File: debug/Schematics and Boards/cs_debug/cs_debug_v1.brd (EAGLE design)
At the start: 38.1 x 44.5 mm, 59 parts, among them J401 J-USB-HIROSE-MICRO-USB, Y101 32.768kHz, Y102 12mHz-12pF-K7

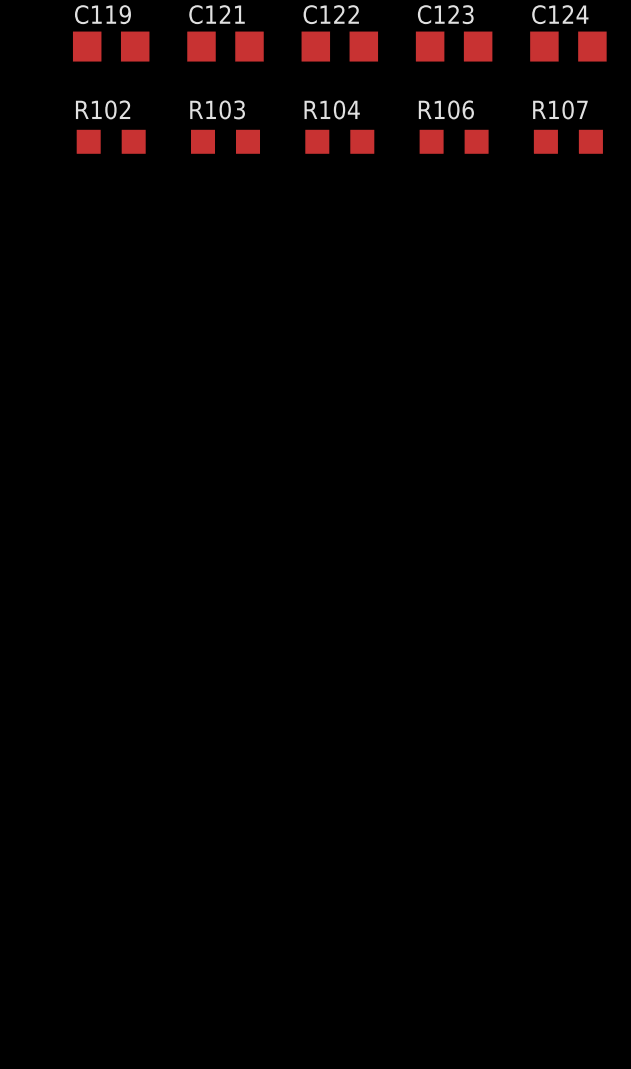
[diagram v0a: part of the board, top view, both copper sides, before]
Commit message: Add amplifiers and passives for high-side current monitor
FETs still to be added. Haven't set values on passives or added any part numbers to the circuit. Still need to convert the whole thing into a group. The nets have been named, and a few notes left behind for the remaining task
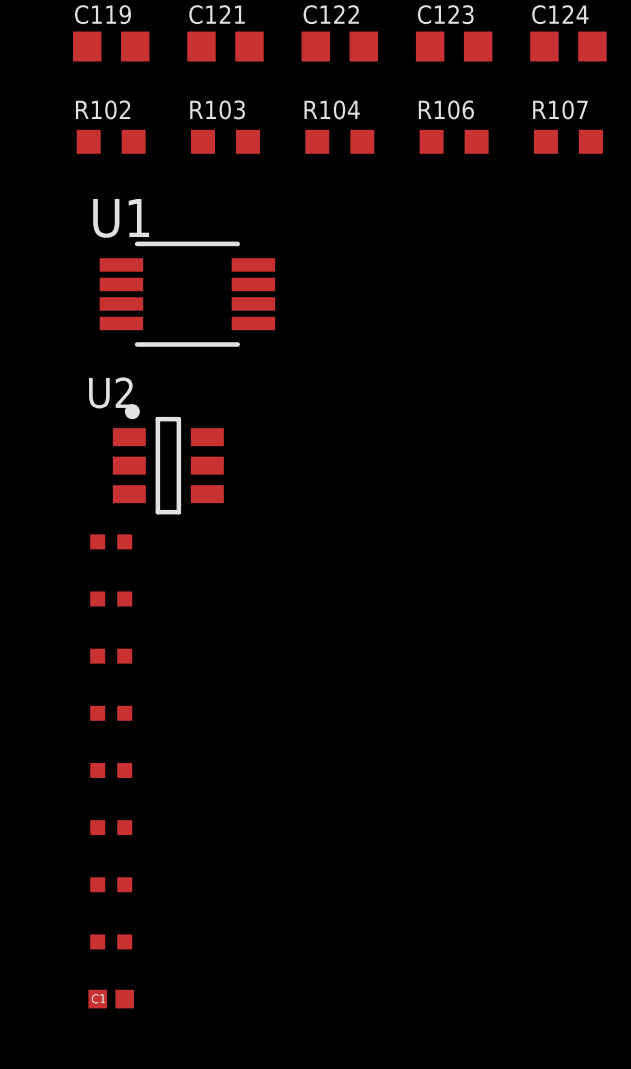
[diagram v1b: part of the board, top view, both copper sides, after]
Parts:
- added C1: (no value), Capacitors:C0402
- added R1, R2, R3, R4, R5, R6, R7, R8: (no value), Resistors:R0402
- added U1: INA225AIDGK, Amplifiers:DGK-MSOP8_INA225
- added U2: OPA357AIDBVTG4, Amplifiers:OPA357AIDBVTG4
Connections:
- new net AGND: R5.1, U1.GND, U1.REF, U2.VREF-
- new net DCBIAS_SHUTDOWN: R6.1
- new net DIFFAMP_GAIN0: U1.GS0
- new net DIFFAMP_GAIN1: U1.GS1
- new net N$1: R1.2, R2.2, U2.IN+
- new net N$3: U1.OUT
- new net N$4: R3.1, U2.ENABLE
- new net N$6: R4.1, R5.2, U2.IN-
- new net N$7: R4.2, R7.1, U2.OUT
- new net N$8: C1.2, R8.2, U1.IN+
- new net N$9: C1.1, R7.2, U1.IN-
- new net V_OFFSET_IN: R1.1
- new net V_SENSE_N: R2.1
- new net V_SENSE_P: R8.1
- net 3V3_INSTR_PROC: now also R3.2, R6.2, U1.VS, U2.VREF+

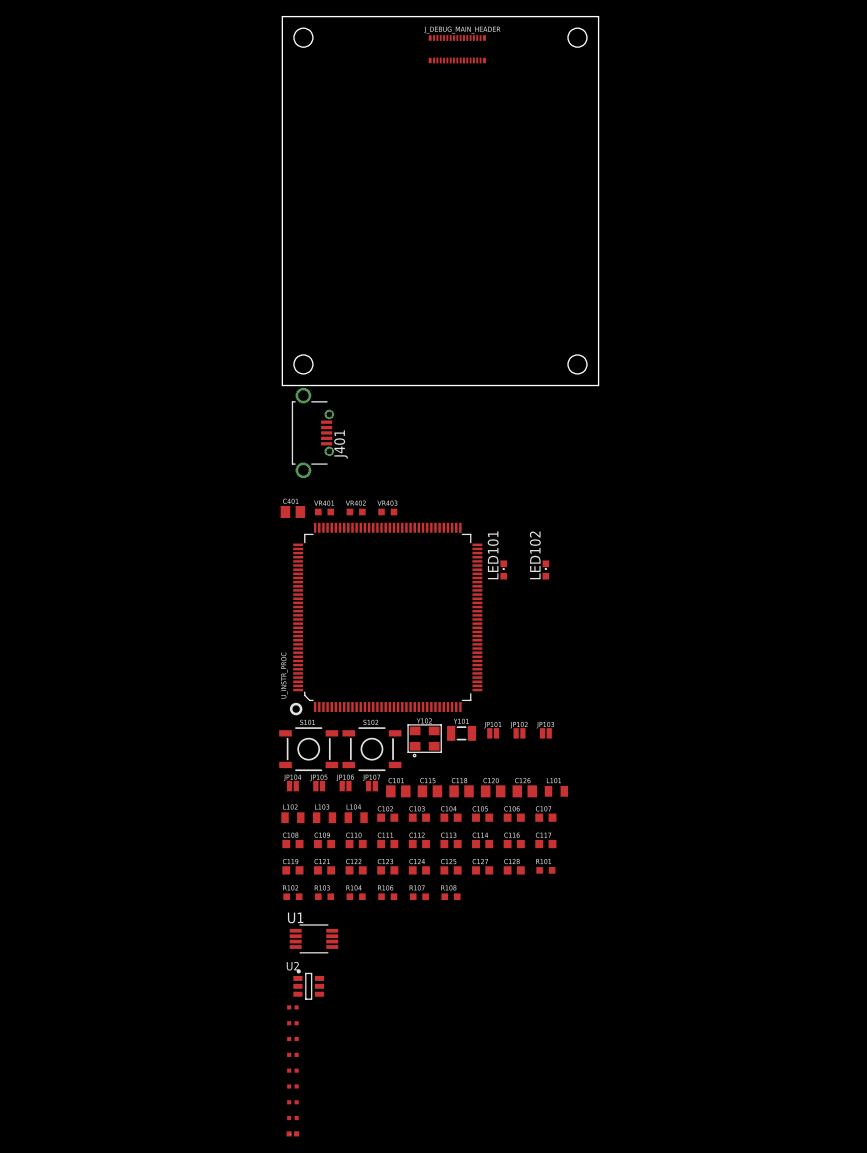
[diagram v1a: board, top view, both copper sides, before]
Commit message: Add high side current monitors as groups; label pins from main connector
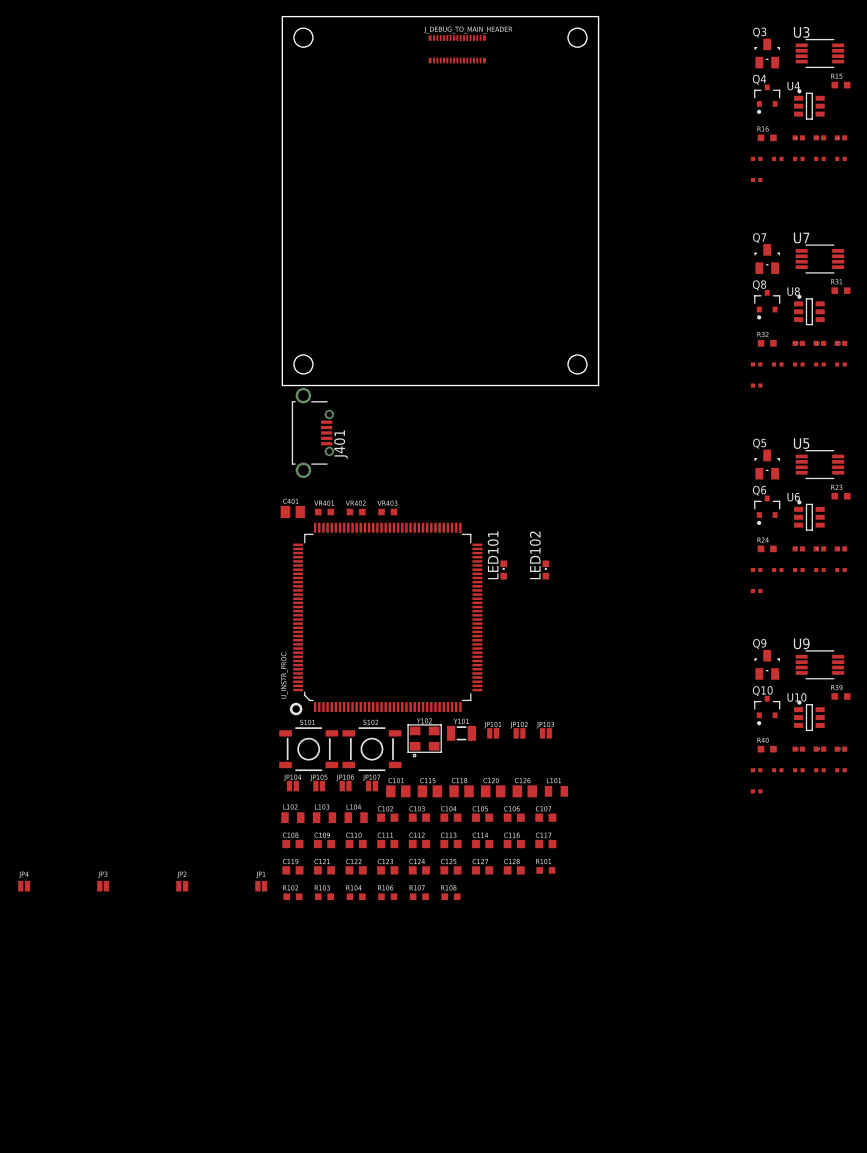
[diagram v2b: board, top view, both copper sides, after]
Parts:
- removed C1: (no value), Capacitors:C0402
- removed R1, R2, R3, R4, R5, R6, R7, R8: (no value), Resistors:R0402
- removed U1: INA225AIDGK, Amplifiers:DGK-MSOP8_INA225
- removed U2: OPA357AIDBVTG4, Amplifiers:OPA357AIDBVTG4
- added C10, C13, C4, C7: 68p, Capacitors:C0402
- added C11, C12, C14, C15, C5, C6, C8, C9: 0.1u, Capacitors:C0402
- added JP1, JP2, JP3, JP4: JUMPER-SMT_2_NC_PASTE_NO-SILK, SparkFun-Jumpers:SMT-JUMPER_2_NC_PASTE_NO-SILK
- added Q10, Q4, Q6, Q8: 2N7002P, Switches:SOT23-3_2N7002P
- added Q3, Q5, Q7, Q9: FDN340P, Switches:SOT23-3_FDN340P
- added R10, R12, R14, R18, R20, R22, R26, R28, R30, R34, R36, R38: 10k, Resistors:R0402
- added R11, R19, R27, R35: 100k, Resistors:R0402
- added R13, R17, R21, R25, R29, R33, R37, R9: 249k, Resistors:R0402
- added R15, R16, R23, R24, R31, R32, R39, R40: 5.1, Resistors:R0603
- added U10, U4, U6, U8: OPA357AIDBVTG4, Amplifiers:OPA357AIDBVTG4
- added U3, U5, U7, U9: INA225AIDGK, Amplifiers:DGK-MSOP8_INA225
- renumbered J_DEBUG_MAIN_HEADER to J_DEBUG_TO_MAIN_HEADER
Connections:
- removed net DCBIAS_SHUTDOWN: R6.1
- removed net DIFFAMP_GAIN0: U1.GS0
- removed net DIFFAMP_GAIN1: U1.GS1
- removed net N$1: R1.2, R2.2, U2.IN+
- removed net N$3: U1.OUT
- removed net N$4: R3.1, U2.ENABLE
- removed net N$6: R4.1, R5.2, U2.IN-
- removed net N$7: R4.2, R7.1, U2.OUT
- removed net N$8: C1.2, R8.2, U1.IN+
- removed net N$9: C1.1, R7.2, U1.IN-
- removed net V_OFFSET_IN: R1.1
- removed net V_SENSE_N: R2.1
- new net CM_DTR_DCBIAS_SHUTDOWN: Q8.G, R30.1
- new net CM_DTR_DIFFAMP_GAIN0: U7.GS0
- new net CM_DTR_DIFFAMP_GAIN1: U7.GS1
- new net CM_DTR_DIFFAMP_N3: C10.1, R31.2, U7.IN-
- new net CM_DTR_DIFFAMP_OUT: U7.OUT
- new net CM_DTR_DIFFAMP_P3: C10.2, R32.2, U7.IN+
- new net CM_DTR_OPAMP_ENABLE3: Q7.G, Q8.D, R27.1, U8.ENABLE
- new net CM_DTR_OPAMP_N3: R28.1, R29.2, U8.IN-
- new net CM_DTR_OPAMP_OUT3: Q7.S, R28.2, R31.1, U8.OUT
- new net CM_DTR_OPAMP_P3: R25.2, R26.2, U8.IN+
- new net CM_DTR_V_OFFSET_IN: R25.1
- new net CM_DTR_V_SENSE_N: J_DEBUG_TO_MAIN_HEADER.16, Q7.D, R26.1
- new net CM_DTR_V_SENSE_P: JP4.2, R32.1
- new net CM_PROC_DCBIAS_SHUTDOWN: Q4.G, R14.1
- new net CM_PROC_DIFFAMP_GAIN0: U3.GS0
- new net CM_PROC_DIFFAMP_GAIN1: U3.GS1
- new net CM_PROC_DIFFAMP_N1: C4.1, R15.2, U3.IN-
- new net CM_PROC_DIFFAMP_OUT: U3.OUT
- new net CM_PROC_DIFFAMP_P1: C4.2, R16.2, U3.IN+
- new net CM_PROC_OPAMP_ENABLE1: Q3.G, Q4.D, R11.1, U4.ENABLE
- new net CM_PROC_OPAMP_N1: R12.1, R13.2, U4.IN-
- new net CM_PROC_OPAMP_OUT1: Q3.S, R12.2, R15.1, U4.OUT
- new net CM_PROC_V_OFFSET_IN: R9.1
- new net CM_PROC_V_SENSE_N: J_DEBUG_TO_MAIN_HEADER.14, Q3.D, R10.1
- new net CM_PROC_V_SENSE_P: JP1.2, R16.1
- new net CM_STORAGE_DCBIAS_SHUTDOWN: Q6.G, R22.1
- new net CM_STORAGE_DIFFAMP_GAIN0: U5.GS0
- new net CM_STORAGE_DIFFAMP_GAIN1: U5.GS1
- new net CM_STORAGE_DIFFAMP_N1: C7.1, R23.2, U5.IN-
- new net CM_STORAGE_DIFFAMP_OUT: U5.OUT
- new net CM_STORAGE_DIFFAMP_P1: C7.2, R24.2, U5.IN+
- new net CM_STORAGE_OPAMP_ENABLE1: Q5.G, Q6.D, R19.1, U6.ENABLE
- new net CM_STORAGE_OPAMP_N1: R20.1, R21.2, U6.IN-
- new net CM_STORAGE_OPAMP_OUT1: Q5.S, R20.2, R23.1, U6.OUT
- new net CM_STORAGE_OPAMP_P1: R17.2, R18.2, U6.IN+
- new net CM_STORAGE_V_OFFSET_IN: R17.1
- new net CM_STORAGE_V_SENSE_N: J_DEBUG_TO_MAIN_HEADER.18, Q5.D, R18.1
- new net CM_STORAGE_V_SENSE_P: JP2.2, R24.1
- new net CM_TEMP_DCBIAS_SHUTDOWN: Q10.G, R38.1
- new net CM_TEMP_DIFFAMP_GAIN0: U9.GS0
- new net CM_TEMP_DIFFAMP_GAIN1: U9.GS1
- new net CM_TEMP_DIFFAMP_N1: C13.1, R39.2, U9.IN-
- new net CM_TEMP_DIFFAMP_OUT: U9.OUT
- new net CM_TEMP_DIFFAMP_P1: C13.2, R40.2, U9.IN+
- new net CM_TEMP_OPAMP_ENABLE1: Q10.D, Q9.G, R35.1, U10.ENABLE
- new net CM_TEMP_OPAMP_N1: R36.1, R37.2, U10.IN-
- new net CM_TEMP_OPAMP_OUT1: Q9.S, R36.2, R39.1, U10.OUT
- new net CM_TEMP_OPAMP_P1: R33.2, R34.2, U10.IN+
- new net CM_TEMP_V_OFFSET_IN: R33.1
- new net CM_TEMP_V_SENSE_N: J_DEBUG_TO_MAIN_HEADER.20, Q9.D, R34.1
- new net CM_TEMP_V_SENSE_P: JP3.2, R40.1
- new net CM__PROCOPAMP_P1: R10.2, R9.2, U4.IN+
- new net MAIN_GPIO0: J_DEBUG_TO_MAIN_HEADER.7
- new net MAIN_GPIO1: J_DEBUG_TO_MAIN_HEADER.9
- new net MAIN_GPIO2: J_DEBUG_TO_MAIN_HEADER.11
- new net MAIN_GPIO3: J_DEBUG_TO_MAIN_HEADER.13
- new net MAIN_NRESET: J_DEBUG_TO_MAIN_HEADER.30
- new net MAIN_SWD_SWCLK: J_DEBUG_TO_MAIN_HEADER.19
- new net MAIN_SWD_SWDIO: J_DEBUG_TO_MAIN_HEADER.21
- new net MAIN_TRACE_CLK: J_DEBUG_TO_MAIN_HEADER.26
- new net MAIN_TRACE_D0: J_DEBUG_TO_MAIN_HEADER.23
- new net MAIN_TRACE_D1: J_DEBUG_TO_MAIN_HEADER.25
- new net MAIN_TRACE_D2: J_DEBUG_TO_MAIN_HEADER.27
- new net MAIN_TRACE_D3: J_DEBUG_TO_MAIN_HEADER.29
- new net MAIN_TRACE_SWO: J_DEBUG_TO_MAIN_HEADER.28
- new net MAIN_USART_RX: J_DEBUG_TO_MAIN_HEADER.17
- new net MAIN_USART_TX: J_DEBUG_TO_MAIN_HEADER.15
- new net MAIN_USB_DATA_N: J_DEBUG_TO_MAIN_HEADER.22
- new net MAIN_USB_DATA_P: J_DEBUG_TO_MAIN_HEADER.24
- new net VDD_TO_MAIN: J_DEBUG_TO_MAIN_HEADER.2, J_DEBUG_TO_MAIN_HEADER.4
- new net V_BATT_MAIN: J_DEBUG_TO_MAIN_HEADER.10, J_DEBUG_TO_MAIN_HEADER.6, J_DEBUG_TO_MAIN_HEADER.8
- net 3V3_INSTR_PROC: now also C11.1, C12.1, C14.1, C15.1, C5.1, C6.1, C8.1, C9.1, R11.2, R14.2, R19.2, R22.2, R27.2, R30.2, R35.2, R38.2, U10.VREF+, U3.VS, U4.VREF+, U5.VS, U6.VREF+, U7.VS, U8.VREF+, U9.VS; no longer R3.2, R6.2, U1.VS, U2.VREF+
- net AGND: now also C11.2, C12.2, C14.2, C15.2, C5.2, C6.2, C8.2, C9.2, Q10.S, Q4.S, Q6.S, Q8.S, R13.1, R21.1, R29.1, R37.1, U10.VREF-, U3.GND, U3.REF, U4.VREF-, U5.GND, U5.REF, U6.VREF-, U7.GND, U7.REF, U8.VREF-, U9.GND, U9.REF; no longer R5.1, U1.GND, U1.REF, U2.VREF-
- net DGND: now also J_DEBUG_TO_MAIN_HEADER.1, J_DEBUG_TO_MAIN_HEADER.3, J_DEBUG_TO_MAIN_HEADER.5
- net V_SENSE_P: now also JP1.1, JP2.1, JP3.1, JP4.1, J_DEBUG_TO_MAIN_HEADER.12; no longer R8.1

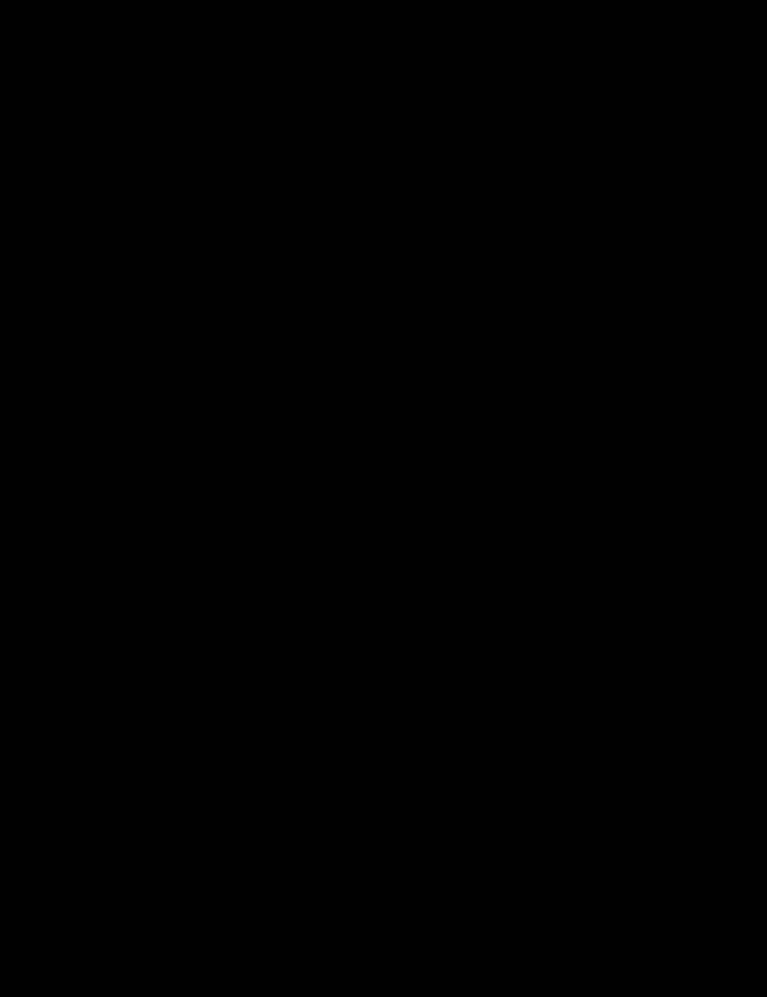
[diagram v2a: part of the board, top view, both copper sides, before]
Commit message: Add LDOs, update formatting
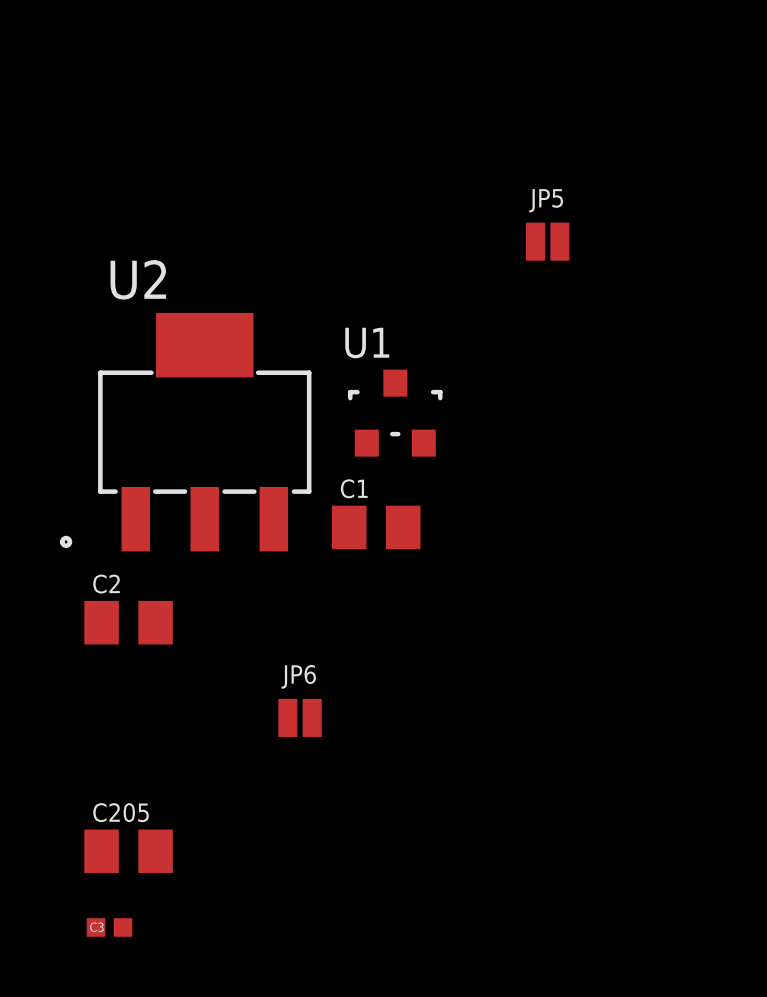
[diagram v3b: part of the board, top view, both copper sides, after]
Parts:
- added C1, C2: 10u, Capacitors:C0805
- added C205: 22u, Capacitors:C0805
- added C3: 0.1u, Capacitors:C0402
- added JP5, JP6: JUMPER-SMT_2_NC_PASTE_NO-SILK, SparkFun-Jumpers:SMT-JUMPER_2_NC_PASTE_NO-SILK
- added U1: AP2120N-3.3TRG1, Regulators:SOT23-3_AP2120N
- added U2: TLV1117LV33DCYR, Regulators:DCY4
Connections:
- new net 3V3_INSTR_MEAS: C1.1, C11.1, C12.1, C14.1, C15.1, C5.1, C6.1, C8.1, C9.1, R11.2, R14.2, R19.2, R22.2, R27.2, R30.2, R35.2, R38.2, U1.OUT, U10.VREF+, U3.VS, U4.VREF+, U5.VS, U6.VREF+, U7.VS, U8.VREF+, U9.VS
- new net N$1: JP5.2, U1.IN
- new net N$3: C205.1, C3.1, JP5.1, JP6.1
- new net N$4: JP6.2, U2.IN
- new net N$6: U_INSTR_PROC.28
- new net N$7: U_INSTR_PROC.29
- new net N$8: U_INSTR_PROC.30
- new net N$9: U_INSTR_PROC.31
- net 3V3_INSTR_PROC: now also C2.1, U2.OUT, U2.OUT_TAB; no longer C11.1, C12.1, C14.1, C15.1, C5.1, C6.1, C8.1, C9.1, R11.2, R14.2, R19.2, R22.2, R27.2, R30.2, R35.2, R38.2, U10.VREF+, U3.VS, U4.VREF+, U5.VS, U6.VREF+, U7.VS, U8.VREF+, U9.VS
- net AGND: now also C1.2, U1.GND
- net DGND: now also C2.2, C205.2, C3.2, U2.GND
